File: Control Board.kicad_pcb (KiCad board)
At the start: 2 copper layers, 154 x 175 mm, 90 parts, among them J1 ED2627-ND, J10 6posheader, J11 S7038-ND, J12 ED2989-ND-USB, J13 ED1501-ND, J14 ED2989-ND-USB, J15 ED2580-ND, J16 ED2580-ND, J17 ED2744-ND, J18 ED2744-ND, J19 ED2744-ND, J2 ED2627-ND, J20 ED2744-ND, J21 ED2744-ND, J22 ED2744-ND, J23 ED2744-ND, J24 ED2744-ND, J25 ED2744-ND, J26 ED2744-ND, J3 ED2627-ND, J4 ED2627-ND, J5 ED2627-ND, J6 S9175-ND, J7 S9175-ND, J8 6posheader, J9 S7038-ND, M1 Mounting_Holes, T1 test_point, T10 test_point, T11 test_point, T12 test_point, T13 test_point, T14 test_point, T15 test_point, T16 test_point, T17 test_point, T18 test_point, T19 test_point, T2 test_point, T20 test_point, T21 test_point, T3 test_point, T4 test_point, T5 test_point, T6 test_point, T7 test_point, T8 test_point, T9 test_point, U1 LM358-N, U2 LM358-N, y1 rover_silkscreen

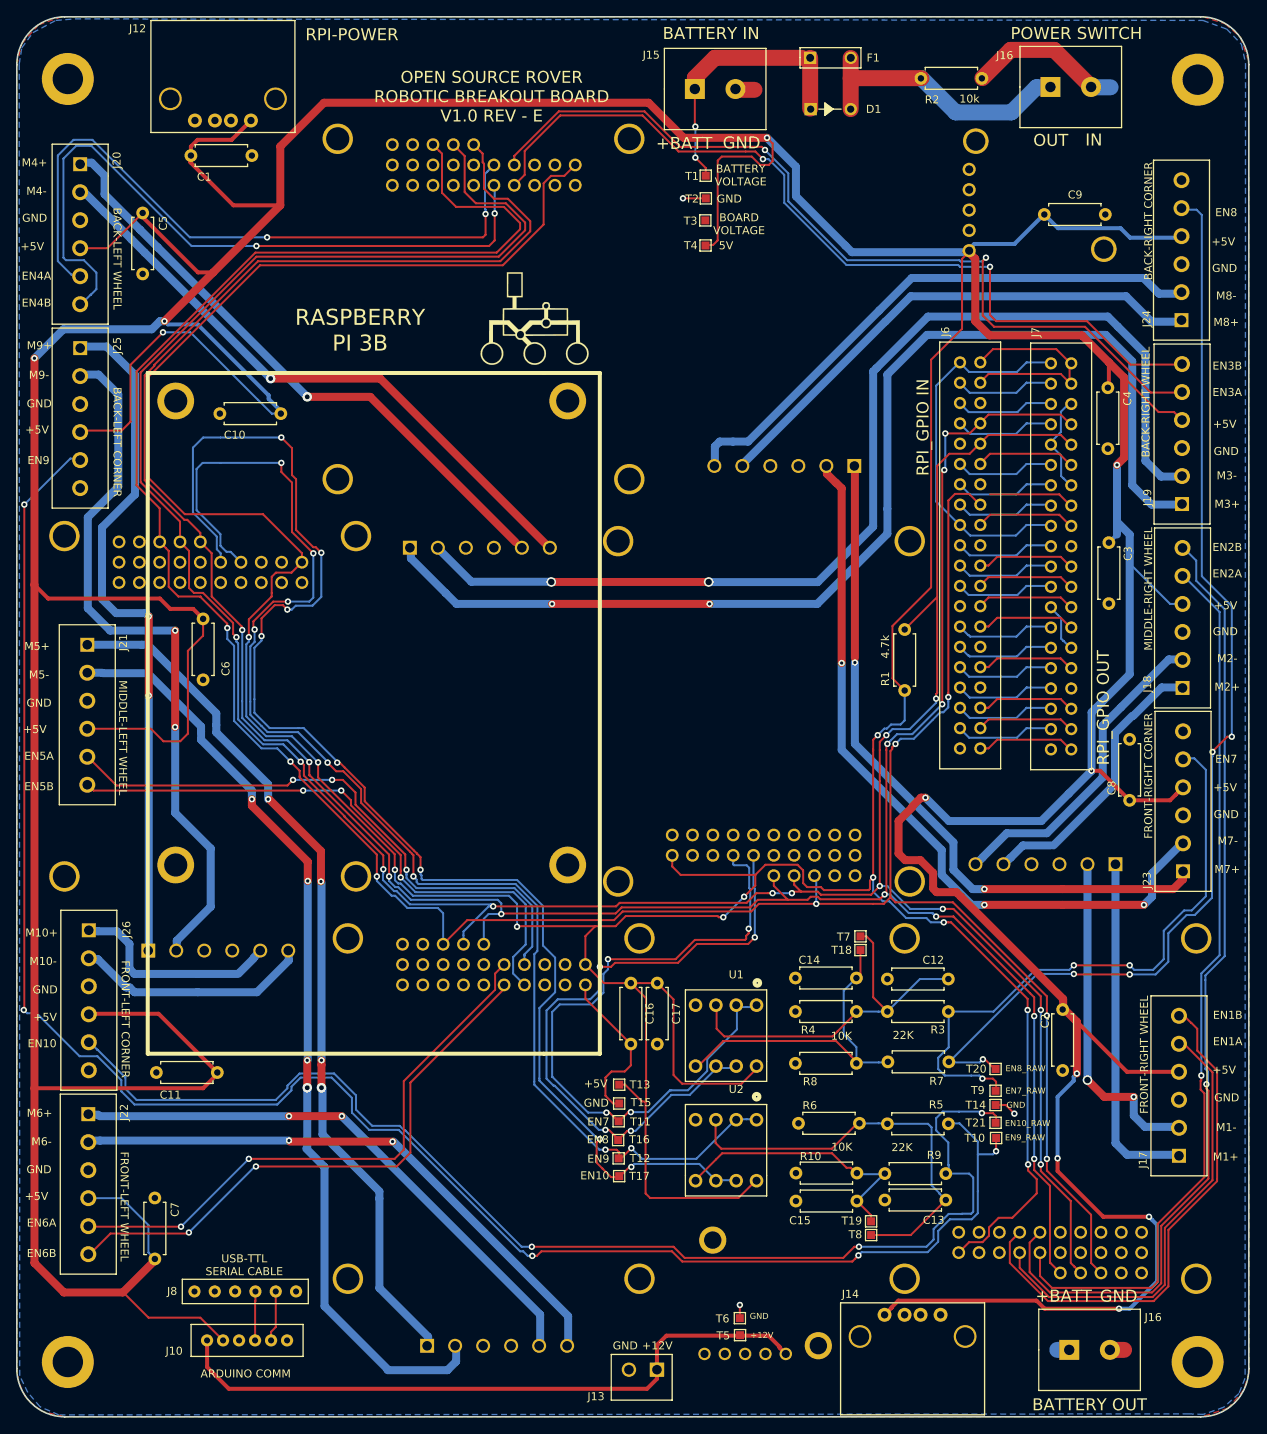
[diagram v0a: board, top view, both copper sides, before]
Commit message: Added JST connectors, screw terminals, and widened traces
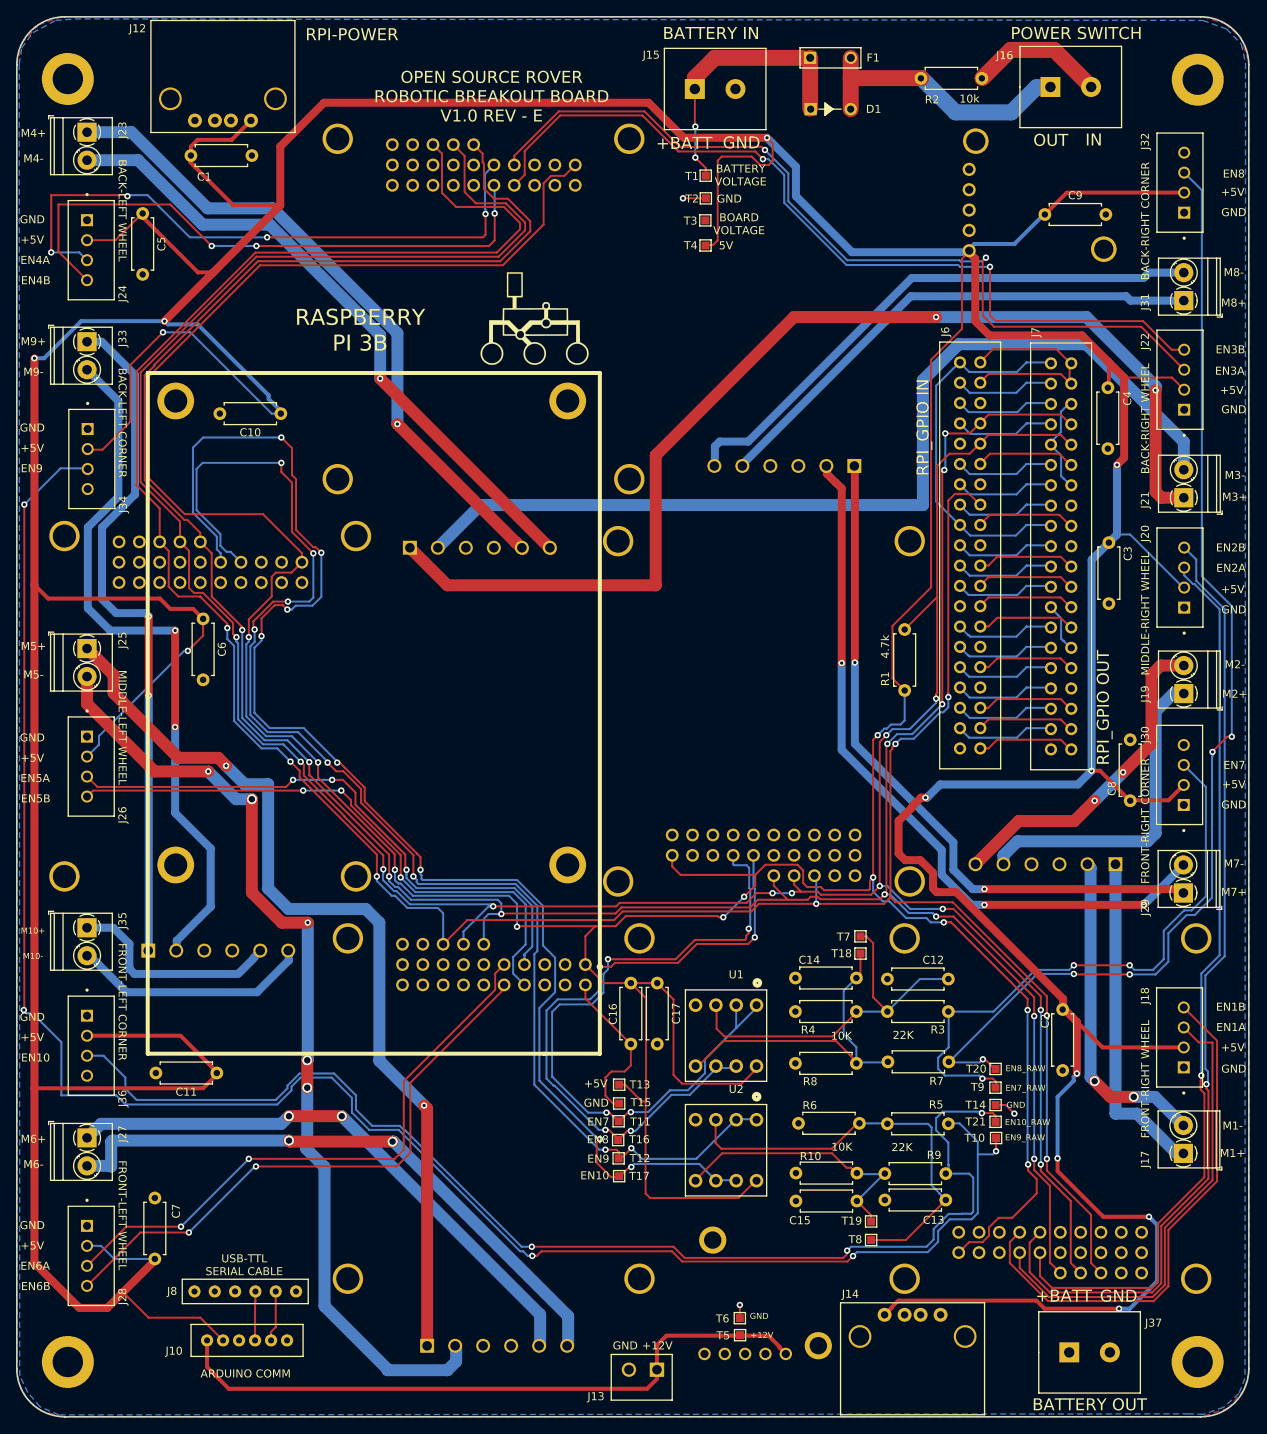
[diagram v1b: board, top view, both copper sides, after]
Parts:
- removed the J16 at (130.6, -7.37)
- added J27: Conn_01x02, TerminalBlock_Phoenix:TerminalBlock_Phoenix_PT-1,5-2-3.5-H_1x02_P3.50mm_Horizontal, F.Cu at (7.78, -33.9)
- added J28: Conn_01x04, Connector_JST:JST_B4B-XH-A(LF)(SN), F.Cu at (8.30, -19.1)
- added J29: Conn_01x02, TerminalBlock_Phoenix:TerminalBlock_Phoenix_PT-1,5-2-3.5-H_1x02_P3.50mm_Horizontal, F.Cu at (144.8, -64.5)
- added J30: Conn_01x04, Connector_JST:JST_B4B-XH-A(LF)(SN), F.Cu at (144.3, -79.2)
- added J31: Conn_01x02, TerminalBlock_Phoenix:TerminalBlock_Phoenix_PT-1,5-2-3.5-H_1x02_P3.50mm_Horizontal, F.Cu at (144.9, -138.5)
- added J32: Conn_01x04, Connector_JST:JST_B4B-XH-A(LF)(SN), F.Cu at (144.4, -153.3)
- added J33: Conn_01x02, TerminalBlock_Phoenix:TerminalBlock_Phoenix_PT-1,5-2-3.5-H_1x02_P3.50mm_Horizontal, F.Cu at (7.78, -133.4)
- added J34: Conn_01x04, Connector_JST:JST_B4B-XH-A(LF)(SN), F.Cu at (8.38, -118.7)
- added J35: Conn_01x02, TerminalBlock_Phoenix:TerminalBlock_Phoenix_PT-1,5-2-3.5-H_1x02_P3.50mm_Horizontal, F.Cu at (7.78, -60.1)
- added J36: Conn_01x04, Connector_JST:JST_B4B-XH-A(LF)(SN), F.Cu at (8.30, -45.4)
- added J37: ED2580-ND, JPL Robotics:ED2580-ND, F.Cu at (130.6, -7.05)
- J17, J19, J21, J23, J25: value ED2744-ND -> Conn_01x02; footprint JPL Robotics:ED2744-ND -> TerminalBlock_Phoenix:TerminalBlock_Phoenix_PT-1,5-2-3.5-H_1x02_P3.50mm_Horizontal
- J18, J20, J22, J24, J26: value ED2744-ND -> Conn_01x04; footprint JPL Robotics:ED2744-ND -> Connector_JST:JST_B4B-XH-A(LF)(SN)
- moved J23 165.2 mm to (7.78, -159.6), turned to -90 degrees
- moved J22 164.5 mm to (144.4, -128.6), turned to 90 degrees
- moved J20 146.9 mm to (144.4, -103.9), turned to 90 degrees
- moved J21 138.3 mm to (144.9, -113.9), turned to 90 degrees
- moved J24 136.6 mm to (8.30, -144.8), turned to -90 degrees
- moved J18 43.7 mm to (144.3, -46.4)
- moved J25 37.6 mm to (7.78, -95.0)
- moved J19 23.7 mm to (144.9, -89.4)
- moved J26 20.5 mm to (8.30, -80.3)
- moved J17 0.63 mm to (144.8, -31.9)
- moved T8 0.62 mm to (105.8, -21.1)
- moved T18 0.43 mm to (104.5, -56.9)
- moved T9 0.39 mm to (121.3, -40.1)
- moved T21 0.13 mm to (121.3, -35.9)
- moved C8 0.09 mm to (138.2, -76.0)
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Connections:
- J10 pad 6: Net-(J10-Pad6) -> unconnected-(J10-Pad6)
- J12 pad 2: Net-(J12-Pad2) -> unconnected-(J12-Pad2)
- J12 pad 3: Net-(J12-Pad3) -> unconnected-(J12-Pad3)
- J14 pad 2: Net-(J14-Pad2) -> unconnected-(J14-Pad2)
- J14 pad 3: Net-(J14-Pad3) -> unconnected-(J14-Pad3)
- J18 pad 1: /RC1M2A -> GND
- J18 pad 2: /RC1M2B -> +5V
- J18 pad 3: GND -> /RC1EN1A
- J18 pad 4: +5V -> /RC1EN1B
- J19 pad 1: /RC2M1A -> /RC1M2A
- J19 pad 2: /RC2M1B -> /RC1M2B
- J20 pad 1: /RC2M2A -> GND
- J20 pad 2: /RC2M2B -> +5V
- J20 pad 3: GND -> /RC1EN2A
- J20 pad 4: +5V -> /RC1EN2B
- J21 pad 1: /RC3M1A -> /RC2M1A
- J21 pad 2: /RC3M1B -> /RC2M1B
- J22 pad 1: /RC3M2A -> GND
- J22 pad 2: /RC3M2B -> +5V
- J22 pad 3: GND -> /RC2EN1A
- J22 pad 4: +5V -> /RC2EN1B
- J23 pad 1: /RC4M1A -> /RC2M2A
- J23 pad 2: /RC4M1B -> /RC2M2B
- J24 pad 1: /RC4M2A -> GND
- J24 pad 2: /RC4M2B -> +5V
- J24 pad 3: GND -> /RC2EN2A
- J24 pad 4: +5V -> /RC2EN2B
- J25 pad 1: /RC5M1A -> /RC3M1A
- J25 pad 2: /RC5M1B -> /RC3M1B
- J26 pad 1: /RC5M2A -> GND
- J26 pad 2: /RC5M2B -> +5V
- J26 pad 3: GND -> /RC3EN1A
- J26 pad 4: +5V -> /RC3EN1B
- J6 pad 14: Net-(J6-Pad14) -> unconnected-(J6-Pad14)
- J6 pad 20: Net-(J6-Pad20) -> unconnected-(J6-Pad20)
- J6 pad 25: Net-(J6-Pad25) -> unconnected-(J6-Pad25)
- J6 pad 30: Net-(J6-Pad30) -> unconnected-(J6-Pad30)
- J6 pad 34: Net-(J6-Pad34) -> unconnected-(J6-Pad34)
- J6 pad 39: Net-(J6-Pad39) -> unconnected-(J6-Pad39)
- J6 pad 6: Net-(J6-Pad6) -> unconnected-(J6-Pad6)
- J6 pad 9: Net-(J6-Pad9) -> unconnected-(J6-Pad9)
- J7 pad 16: Net-(J7-Pad16) -> unconnected-(J7-Pad16)
- J8 pad 3: Net-(J8-Pad3) -> unconnected-(J8-Pad3)
- RC1 pad 11: Net-(RC1-Pad11) -> unconnected-(RC1-Pad11)
- RC1 pad 12: Net-(RC1-Pad12) -> unconnected-(RC1-Pad12)
- RC1 pad 13: Net-(RC1-Pad13) -> unconnected-(RC1-Pad13)
- RC1 pad 14: Net-(RC1-Pad14) -> unconnected-(RC1-Pad14)
- RC1 pad 15: Net-(RC1-Pad15) -> unconnected-(RC1-Pad15)
- RC1 pad 16: Net-(RC1-Pad16) -> unconnected-(RC1-Pad16)
- RC1 pad 17: Net-(RC1-Pad17) -> unconnected-(RC1-Pad17)
- RC1 pad 18: Net-(RC1-Pad18) -> unconnected-(RC1-Pad18)
- RC1 pad 19: Net-(RC1-Pad19) -> unconnected-(RC1-Pad19)
- RC1 pad 20: Net-(RC1-Pad20) -> unconnected-(RC1-Pad20)
- RC1 pad 24: Net-(RC1-Pad24) -> unconnected-(RC1-Pad24)
- RC1 pad 25: Net-(RC1-Pad25) -> unconnected-(RC1-Pad25)
- RC1 pad 3: Net-(RC1-Pad3) -> unconnected-(RC1-Pad3)
- RC1 pad 4: Net-(RC1-Pad4) -> unconnected-(RC1-Pad4)
- RC1 pad 5: Net-(RC1-Pad5) -> unconnected-(RC1-Pad5)
- RC1 pad 6: Net-(RC1-Pad6) -> unconnected-(RC1-Pad6)
- RC2 pad 11: Net-(RC2-Pad11) -> unconnected-(RC2-Pad11)
- RC2 pad 12: Net-(RC2-Pad12) -> unconnected-(RC2-Pad12)
- RC2 pad 13: Net-(RC2-Pad13) -> unconnected-(RC2-Pad13)
- RC2 pad 14: Net-(RC2-Pad14) -> unconnected-(RC2-Pad14)
- RC2 pad 15: Net-(RC2-Pad15) -> unconnected-(RC2-Pad15)
- RC2 pad 16: Net-(RC2-Pad16) -> unconnected-(RC2-Pad16)
- RC2 pad 17: Net-(RC2-Pad17) -> unconnected-(RC2-Pad17)
- RC2 pad 18: Net-(RC2-Pad18) -> unconnected-(RC2-Pad18)
- RC2 pad 19: Net-(RC2-Pad19) -> unconnected-(RC2-Pad19)
- RC2 pad 20: Net-(RC2-Pad20) -> unconnected-(RC2-Pad20)
- RC2 pad 24: Net-(RC2-Pad24) -> unconnected-(RC2-Pad24)
- RC2 pad 25: Net-(RC2-Pad25) -> unconnected-(RC2-Pad25)
- RC2 pad 3: Net-(RC2-Pad3) -> unconnected-(RC2-Pad3)
- RC2 pad 4: Net-(RC2-Pad4) -> unconnected-(RC2-Pad4)
- RC2 pad 5: Net-(RC2-Pad5) -> unconnected-(RC2-Pad5)
- RC2 pad 6: Net-(RC2-Pad6) -> unconnected-(RC2-Pad6)
- RC3 pad 11: Net-(RC3-Pad11) -> unconnected-(RC3-Pad11)
- RC3 pad 12: Net-(RC3-Pad12) -> unconnected-(RC3-Pad12)
- RC3 pad 13: Net-(RC3-Pad13) -> unconnected-(RC3-Pad13)
- RC3 pad 14: Net-(RC3-Pad14) -> unconnected-(RC3-Pad14)
- RC3 pad 15: Net-(RC3-Pad15) -> unconnected-(RC3-Pad15)
- RC3 pad 16: Net-(RC3-Pad16) -> unconnected-(RC3-Pad16)
- RC3 pad 17: Net-(RC3-Pad17) -> unconnected-(RC3-Pad17)
- RC3 pad 18: Net-(RC3-Pad18) -> unconnected-(RC3-Pad18)
- RC3 pad 19: Net-(RC3-Pad19) -> unconnected-(RC3-Pad19)
- RC3 pad 20: Net-(RC3-Pad20) -> unconnected-(RC3-Pad20)
- RC3 pad 24: Net-(RC3-Pad24) -> unconnected-(RC3-Pad24)
- RC3 pad 25: Net-(RC3-Pad25) -> unconnected-(RC3-Pad25)
- RC3 pad 3: Net-(RC3-Pad3) -> unconnected-(RC3-Pad3)
- RC3 pad 4: Net-(RC3-Pad4) -> unconnected-(RC3-Pad4)
- RC3 pad 5: Net-(RC3-Pad5) -> unconnected-(RC3-Pad5)
- RC3 pad 6: Net-(RC3-Pad6) -> unconnected-(RC3-Pad6)
- RC4 pad 10: Net-(RC4-Pad10) -> unconnected-(RC4-Pad10)
- RC4 pad 11: Net-(RC4-Pad11) -> unconnected-(RC4-Pad11)
- RC4 pad 12: Net-(RC4-Pad12) -> unconnected-(RC4-Pad12)
- RC4 pad 13: Net-(RC4-Pad13) -> unconnected-(RC4-Pad13)
- RC4 pad 14: Net-(RC4-Pad14) -> unconnected-(RC4-Pad14)
- RC4 pad 15: Net-(RC4-Pad15) -> unconnected-(RC4-Pad15)
- RC4 pad 16: Net-(RC4-Pad16) -> unconnected-(RC4-Pad16)
- RC4 pad 17: Net-(RC4-Pad17) -> unconnected-(RC4-Pad17)
- RC4 pad 18: Net-(RC4-Pad18) -> unconnected-(RC4-Pad18)
- RC4 pad 19: Net-(RC4-Pad19) -> unconnected-(RC4-Pad19)
- RC4 pad 20: Net-(RC4-Pad20) -> unconnected-(RC4-Pad20)
- RC4 pad 24: Net-(RC4-Pad24) -> unconnected-(RC4-Pad24)
- RC4 pad 25: Net-(RC4-Pad25) -> unconnected-(RC4-Pad25)
- RC4 pad 3: Net-(RC4-Pad3) -> unconnected-(RC4-Pad3)
- RC4 pad 4: Net-(RC4-Pad4) -> unconnected-(RC4-Pad4)
- RC4 pad 5: Net-(RC4-Pad5) -> unconnected-(RC4-Pad5)
- RC4 pad 6: Net-(RC4-Pad6) -> unconnected-(RC4-Pad6)
- RC4 pad 8: Net-(RC4-Pad8) -> unconnected-(RC4-Pad8)
- RC5 pad 10: Net-(RC5-Pad10) -> unconnected-(RC5-Pad10)
- RC5 pad 11: Net-(RC5-Pad11) -> unconnected-(RC5-Pad11)
- RC5 pad 12: Net-(RC5-Pad12) -> unconnected-(RC5-Pad12)
- RC5 pad 13: Net-(RC5-Pad13) -> unconnected-(RC5-Pad13)
- RC5 pad 14: Net-(RC5-Pad14) -> unconnected-(RC5-Pad14)
- RC5 pad 15: Net-(RC5-Pad15) -> unconnected-(RC5-Pad15)
- RC5 pad 16: Net-(RC5-Pad16) -> unconnected-(RC5-Pad16)
- RC5 pad 17: Net-(RC5-Pad17) -> unconnected-(RC5-Pad17)
- RC5 pad 18: Net-(RC5-Pad18) -> unconnected-(RC5-Pad18)
- RC5 pad 19: Net-(RC5-Pad19) -> unconnected-(RC5-Pad19)
- RC5 pad 20: Net-(RC5-Pad20) -> unconnected-(RC5-Pad20)
- RC5 pad 24: Net-(RC5-Pad24) -> unconnected-(RC5-Pad24)
- RC5 pad 25: Net-(RC5-Pad25) -> unconnected-(RC5-Pad25)
- RC5 pad 3: Net-(RC5-Pad3) -> unconnected-(RC5-Pad3)
- RC5 pad 4: Net-(RC5-Pad4) -> unconnected-(RC5-Pad4)
- RC5 pad 5: Net-(RC5-Pad5) -> unconnected-(RC5-Pad5)
- RC5 pad 6: Net-(RC5-Pad6) -> unconnected-(RC5-Pad6)
- RC5 pad 8: Net-(RC5-Pad8) -> unconnected-(RC5-Pad8)
- T14 pad 1: Net-(T14-Pad1) -> GND
- T19 pad 1: Net-(T19-Pad1) -> Net-(C15-Pad2)
- T3 pad 1: Net-(T3-Pad1) -> +BATT
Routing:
- net +5V: track 1316.0 -> 1297.0 mm, vias 22 -> 23
- net /RC2M1B: track 136.0 -> 121.5 mm, vias 2 -> 0
- net /RC2EN2B: track 88.7 -> 74.8 mm, vias 2 -> 3
- net Net-(J7-Pad16): track 10.5 -> 0.00 mm
- net /RC2EN2A: track 85.7 -> 78.0 mm, vias 2 -> 4
- net /RC2M2A: track 76.8 -> 82.7 mm
- net /RC1M2A: track 35.3 -> 41.0 mm
- net /RC3M1A: track 109.9 -> 115.1 mm, vias 4 -> 2
- net /RC2M1A: track 143.6 -> 139.2 mm
- net /RC2M2B: track 77.1 -> 81.3 mm
- net +BATT: track 20.9 -> 17.1 mm
- net /RC4EN2A_RAW: track 141.1 -> 144.7 mm
- net /RC5EN1A_RAW: track 231.6 -> 235.1 mm
- net /RC4M1B: track 94.2 -> 91.2 mm
- net /RC3M2B: track 73.1 -> 76.1 mm
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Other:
- net class Default removed
